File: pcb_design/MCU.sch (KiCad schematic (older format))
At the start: 17 parts, among them J9 SWD, SW1 BOOTLOADER, U1 STM32F40X_LQFP64, X2 ABM3B - 8MHz

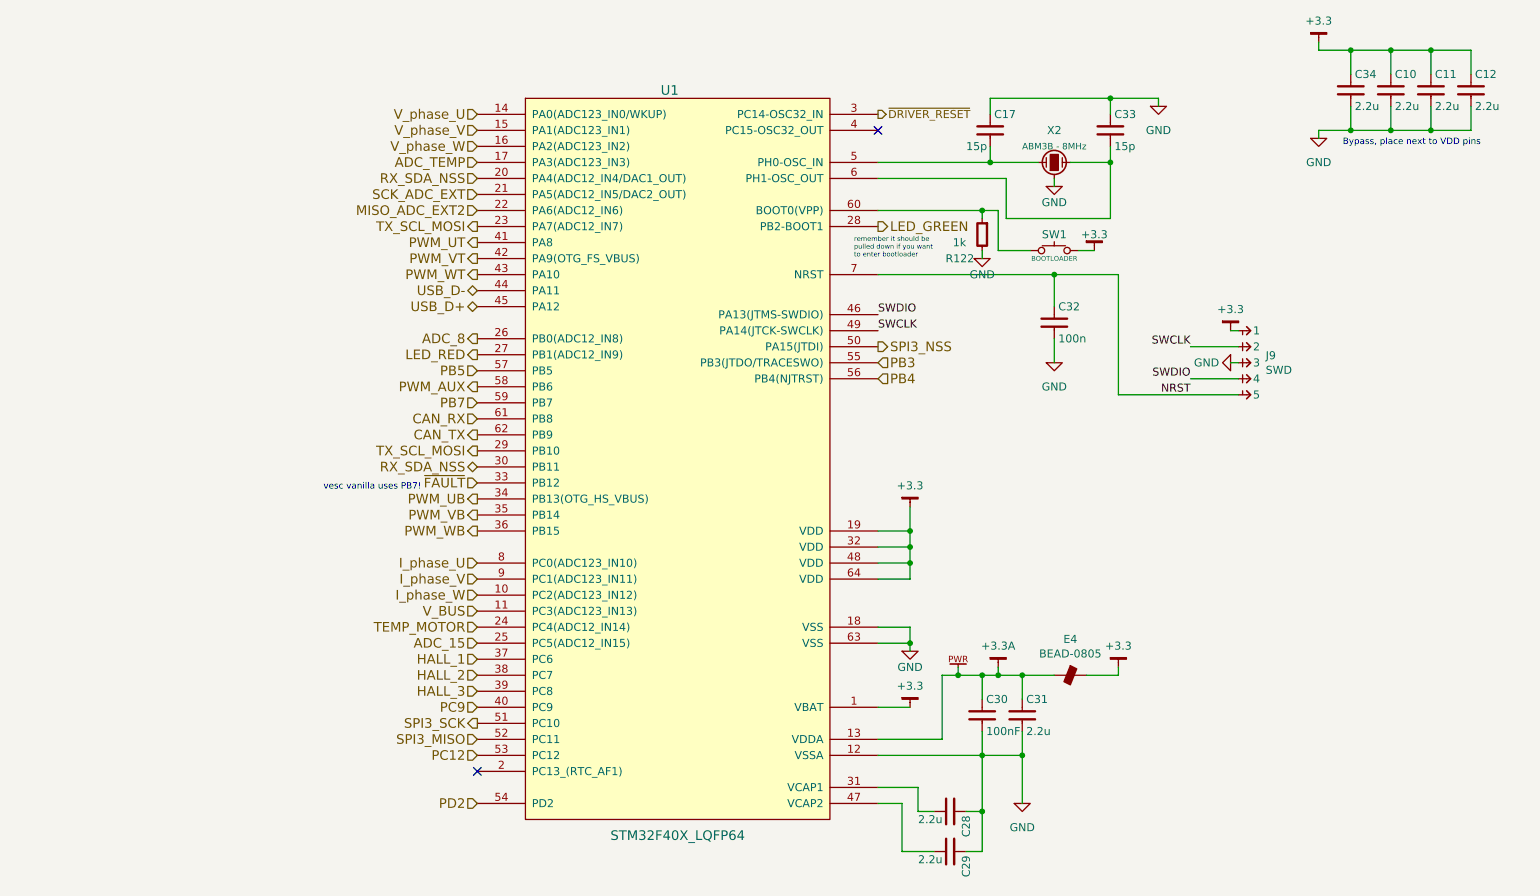
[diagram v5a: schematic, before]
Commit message: Completed some part numbers
Signed-off-by: Marcos Chaparro <mchaparro@paltatech.com>
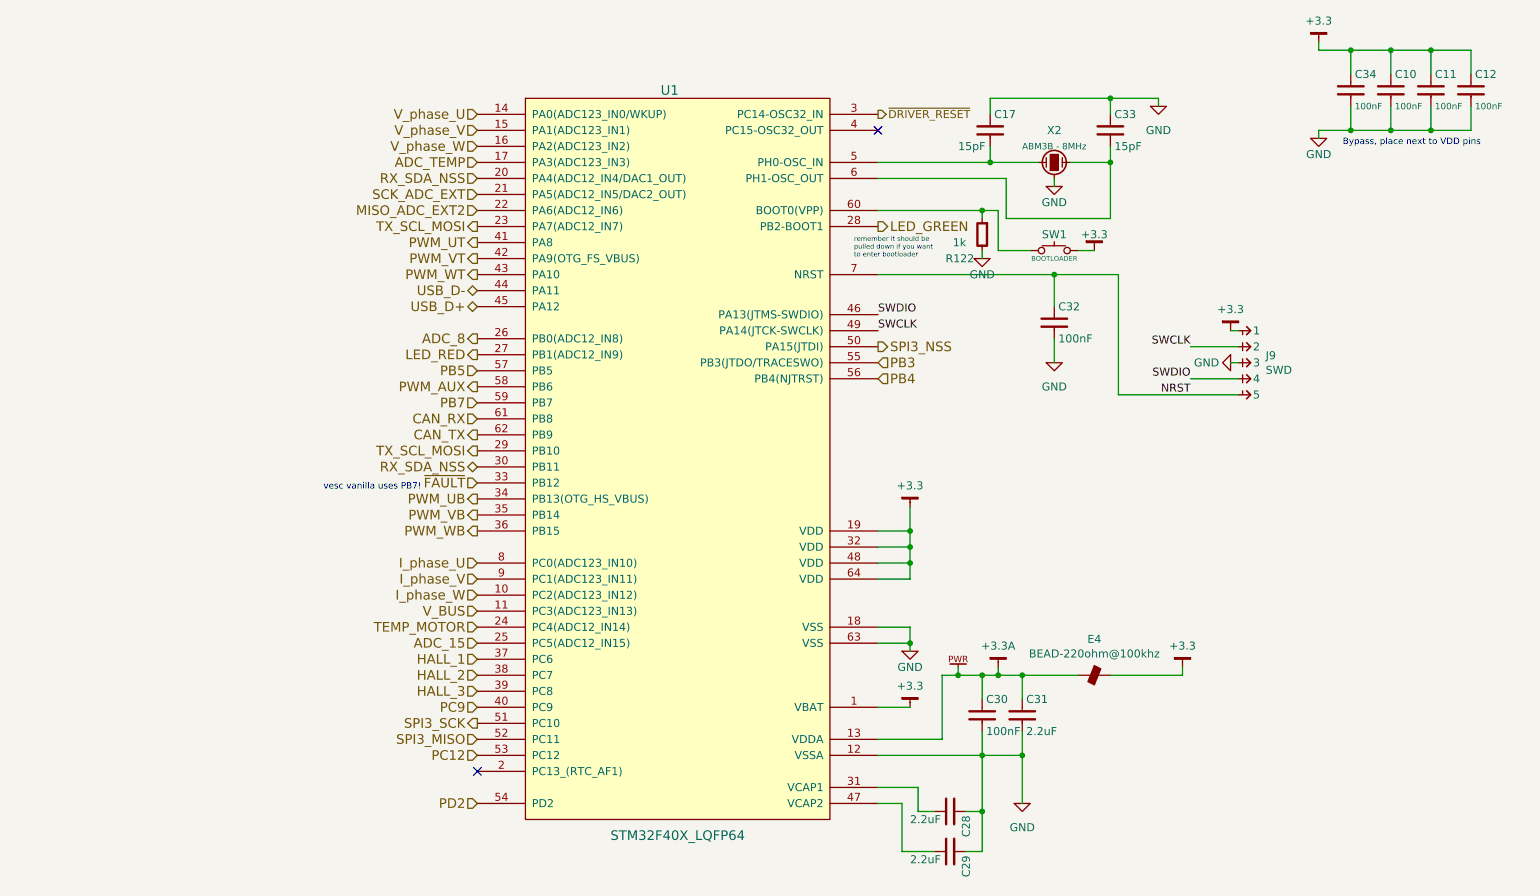
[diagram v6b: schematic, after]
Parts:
- C10, C11, C12, C34: value 2.2u -> 100nF; MFR (none) -> Murata Electronics North America; MPN (none) -> GRM188R71E104KA01D; SPN (none) -> 490-1524-1-ND; SPR (none) -> Digikey
- C17, C33: value 15p -> 15pF; MFR (none) -> Murata Electronics North America; MPN (none) -> GCM1885C1H150JA16D; SPN (none) -> 490-4957-1-ND; SPR (none) -> Digikey
- C28, C29, C31: value 2.2u -> 2.2uF; MFR (none) -> Murata Electronics North America; MPN (none) -> GRM188R71A225KE15D; SPN (none) -> 490-4520-1-ND; SPR (none) -> Digikey
- C30: MFR (none) -> Murata Electronics North America; MPN (none) -> GRM188R71E104KA01D; SPN (none) -> 490-1524-1-ND; SPR (none) -> Digikey
- C32: value 100n -> 100nF; MFR (none) -> Murata Electronics North America; MPN (none) -> GRM188R71E104KA01D; SPN (none) -> 490-1524-1-ND; SPR (none) -> Digikey
- E4: value BEAD-0805 -> BEAD-220ohm@100khz
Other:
- moved on the sheet: E4

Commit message: Completed part number, manufacturer, etc fields. Simulated analog conditioning
Signed-off-by: Marcos Chaparro <mchaparro@paltatech.com>
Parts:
- E4: MFR (none) -> Murata Electronics North America; MPN (none) -> BLM21PG221SN1D; SPN (none) -> 490-1054-1-ND; SPR (none) -> Digikey
- R122: MFR (none) -> Yageo; MPN (none) -> RC0603FR-071KL; SPN (none) -> 311-1.00KHRCT-ND; SPR (none) -> Digikey
- SW1: MFR (none) -> Omron Electronics Inc-EMC Div; MPN (none) -> B3U-1000P; SPN (none) -> SW1020CT-ND; SPR (none) -> Digikey
- U1: MFR (none) -> STMicroelectronics; MPN (none) -> STM32F405RGT6; SPN (none) -> 497-11767-ND; SPR (none) -> Digikey
- X2: MFR (none) -> Abracon LLC; MPN (none) -> ABM3B-8.000MHZ-10-1UT; SPN (none) -> 535-9721-1-ND; SPR (none) -> Digikey
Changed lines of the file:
@@
 F 1 "STM32F40X_LQFP64" H 4900 1300 60 0000 C CNN
 F 2 "IPC7351-Nominal:QFP50P1200X1200X100-64" H 4900 3650 60 0001 C CNN
-F 3 "" H 4900 3650 60 0001 C CNN
-F 4 "" H 0 0 50 0001 C CNN "MFR"
-F 5 "" H 0 0 50 0001 C CNN "MPN"
-F 6 "" H 0 0 50 0001 C CNN "SPR"
-F 7 "" H 0 0 50 0001 C CNN "SPN"
+F 3 "http://www.st.com/content/ccc/resource/technical/document/datasheet/ef/92/76/6d/bb/c2/4f/f7/DM00037051.pdf/files/DM00037051.pdf/jcr:content/translations/en.DM00037051.pdf" H 4900 3650 60 0001 C CNN
+F 4 "STMicroelectronics" H 0 0 50 0001 C CNN "MFR"
+F 5 "STM32F405RGT6" H 0 0 50 0001 C CNN "MPN"
+F 6 "Digikey" H 0 0 50 0001 C CNN "SPR"
+F 7 "497-11767-ND" H 0 0 50 0001 C CNN "SPN"
 F 8 "" H 0 0 50 0001 C CNN "SPURL"
 	1    4900 3650
@@
 F 3 "http://www.abracon.com/Resonators/abm3b.pdf" H 7450 1850 60 0001 C CNN
 F 4 "ABM3B-8.000MHZ-10-1UT" H 7250 1800 60 0001 C CNN "mfg#"
-F 5 "" H 0 0 50 0001 C CNN "MFR"
-F 6 "" H 0 0 50 0001 C CNN "MPN"
-F 7 "" H 0 0 50 0001 C CNN "SPR"
-F 8 "" H 0 0 50 0001 C CNN "SPN"
+F 5 "Abracon LLC" H 0 0 50 0001 C CNN "MFR"
+F 6 "ABM3B-8.000MHZ-10-1UT" H 0 0 50 0001 C CNN "MPN"
+F 7 "Digikey" H 0 0 50 0001 C CNN "SPR"
+F 8 "535-9721-1-ND" H 0 0 50 0001 C CNN "SPN"
 F 9 "" H 0 0 50 0001 C CNN "SPURL"
 	1    7250 1800
@@
 F 1 "BEAD-220ohm@100khz" H 7500 5134 50 0000 C CNN
 F 2 "IPC7351-Nominal:INDC2012X130" H 7500 4900 50 0001 C CNN
-F 3 "" H 7500 5050 60 0000 C CNN
+F 3 "http://search.murata.co.jp/Ceramy/image/img/PDF/ENG/L0110S0100BLM21P.pdf" H 7500 5050 60 0001 C CNN
 F 4 "BEAD SMD 100 @0MHz 1A [0805]" H 7500 4800 60 0001 C CNN "BOM"
-F 5 "" H 0 0 50 0001 C CNN "MFR"
-F 6 "" H 0 0 50 0001 C CNN "MPN"
-F 7 "" H 0 0 50 0001 C CNN "SPR"
-F 8 "" H 0 0 50 0001 C CNN "SPN"
+F 5 "Murata Electronics North America" H 0 0 50 0001 C CNN "MFR"
+F 6 "BLM21PG221SN1D" H 0 0 50 0001 C CNN "MPN"
+F 7 "Digikey" H 0 0 50 0001 C CNN "SPR"
+F 8 "490-1054-1-ND" H 0 0 50 0001 C CNN "SPN"
 F 9 "" H 0 0 50 0001 C CNN "SPURL"
 	1    7500 5000
@@
 F 1 "SWD" H 8569 2604 50 0000 L CNN
 F 2 "conn-100mil:CONN-100MIL-M-1x5" H -100 -550 50 0001 C CNN
-F 3 "" H -100 -550 50 0000 C CNN
+F 3 "" H -100 -550 50 0001 C CNN
 F 4 "" H 0 0 50 0001 C CNN "MFR"
 F 5 "" H 0 0 50 0001 C CNN "MPN"
@@
 F 1 "1k" H 6900 2200 50 0000 L CNN
 F 2 "IPC7351-Nominal:RESC1608X50" H 400 50 50 0001 C CNN
-F 3 "" H 400 100 60 0000 C CNN
+F 3 "" H 400 100 60 0001 C CNN
 F 4 "RES SMD 1k 5% [0603]" H 1150 600 60 0001 C CNN "BOM"
-F 5 "" H 0 0 50 0001 C CNN "MFR"
-F 6 "" H 0 0 50 0001 C CNN "MPN"
-F 7 "" H 0 0 50 0001 C CNN "SPR"
-F 8 "" H 0 0 50 0001 C CNN "SPN"
+F 5 "Yageo" H 0 0 50 0001 C CNN "MFR"
+F 6 "RC0603FR-071KL" H 0 0 50 0001 C CNN "MPN"
+F 7 "Digikey" H 0 0 50 0001 C CNN "SPR"
+F 8 "311-1.00KHRCT-ND" H 0 0 50 0001 C CNN "SPN"
 F 9 "" H 0 0 50 0001 C CNN "SPURL"
 	1    6800 2250
@@
 F 1 "BOOTLOADER" H 7250 2300 30 0000 C CNN
 F 2 "paltatech:SMD-Switch_B3U-1000-B" H 7250 2486 60 0001 C CNN
-F 3 "" H 50 0 60 0000 C CNN
+F 3 "http://www.omron.com/ecb/products/pdf/en-b3u.pdf" H 50 0 60 0001 C CNN
 F 4 "B3U-1000P" H 7250 2350 60 0001 C CNN "mfg#"
-F 5 "" H 0 0 50 0001 C CNN "MFR"
-F 6 "" H 0 0 50 0001 C CNN "MPN"
-F 7 "" H 0 0 50 0001 C CNN "SPR"
-F 8 "" H 0 0 50 0001 C CNN "SPN"
+F 5 "Omron Electronics Inc-EMC Div" H 0 0 50 0001 C CNN "MFR"
+F 6 "B3U-1000P" H 0 0 50 0001 C CNN "MPN"
+F 7 "Digikey" H 0 0 50 0001 C CNN "SPR"
+F 8 "SW1020CT-ND" H 0 0 50 0001 C CNN "SPN"
 F 9 "" H 0 0 50 0001 C CNN "SPURL"
 	1    7250 2350

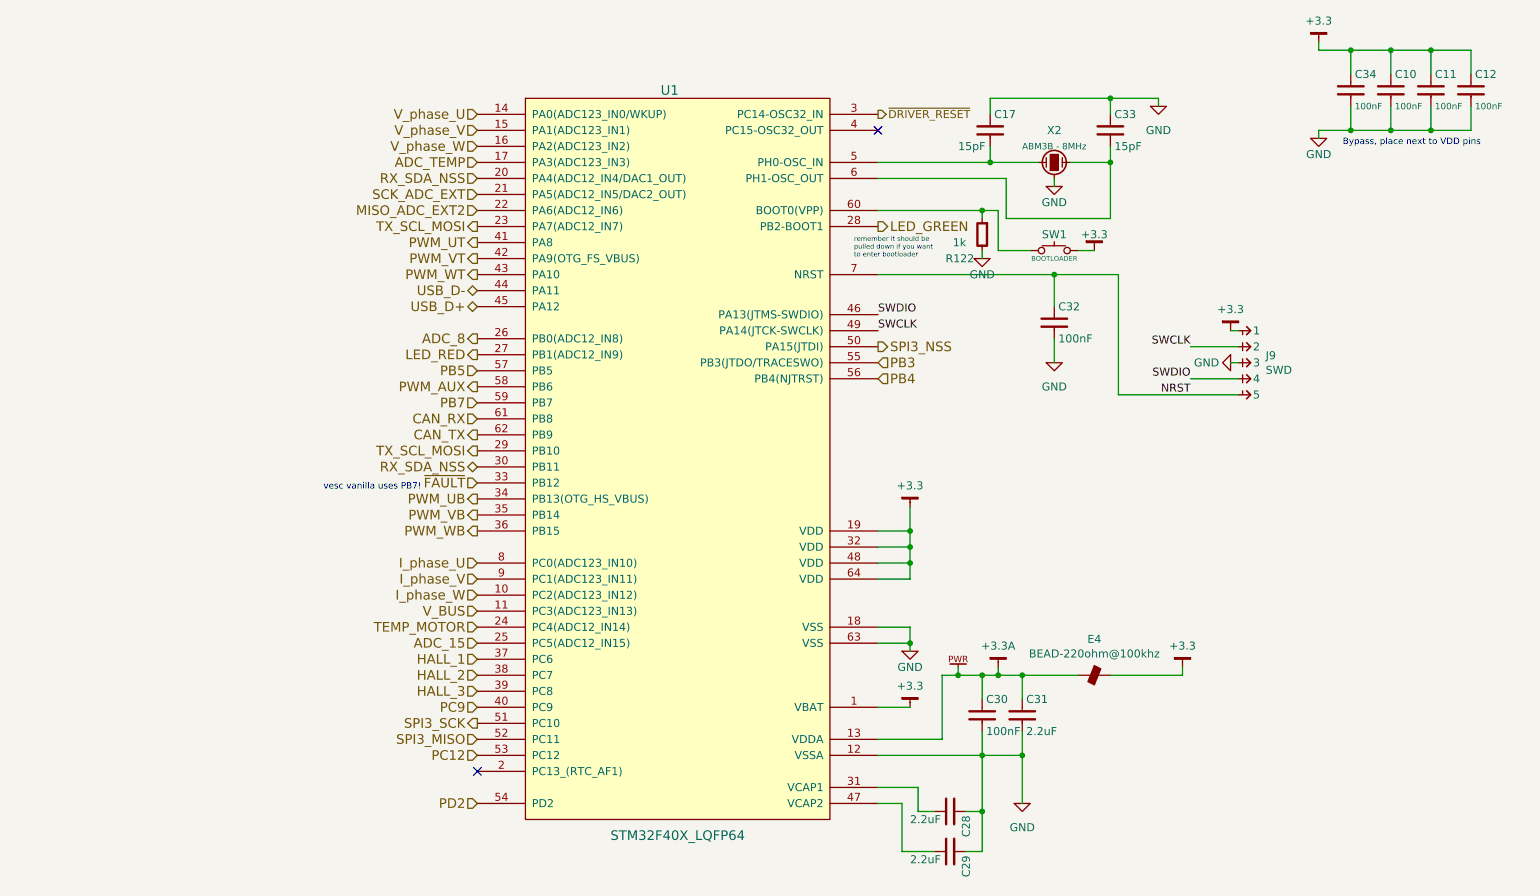
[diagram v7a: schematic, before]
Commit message: Corrected phase current gain. More 3d models
Signed-off-by: Marcos Chaparro <mchaparro@paltatech.com>
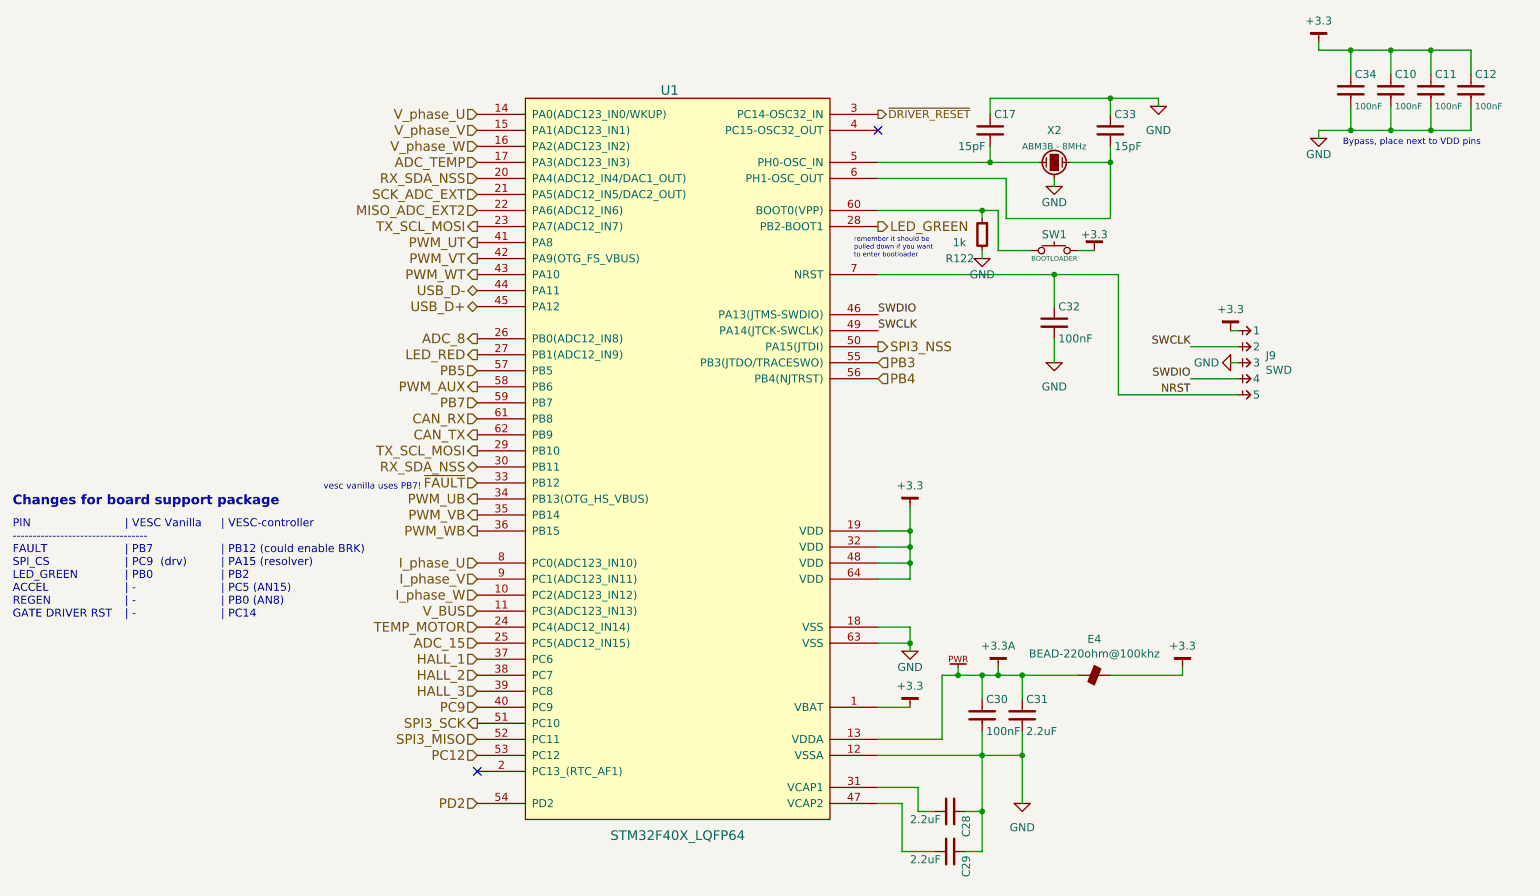
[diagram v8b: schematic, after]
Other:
- note added: "Changes for board support package"
- note added: "\nPIN \n----------------------------------\nFAULT \nSPI_CS\nLED_GREEN\nACCEL\nREGEN\nGATE DRIVER RST"
- note added: "\n| VESC Vanilla\n\n| PB7\n| PC9 (drv)\n| PB0\n| -\n| -\n| -"
- note added: "\n| VESC-controller\n\n| PB12 (could enable BRK)\n| PA15 (resolver)\n| PB2\n| PC5 (AN15)\n| PB0 (AN8)\n| PC14"
